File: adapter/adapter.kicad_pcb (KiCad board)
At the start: 2 copper layers, 41.8 x 50.8 mm, 31 parts, among them J1 Serial, J2 Ribbon, J3 RGB, J4 Ribbon, J5 Battery charge, SW1 SW_SPST, SW3 SW_SPDT, U1 Dual MCU: RP2040 + nice!nano, U2 AP1603WG-7

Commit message: pcb: update pcb from schematic
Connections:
- R1 pad 1: +5V -> +3V3
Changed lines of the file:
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@@
 		(tags "net tie solder jumper bridged")
 		(property "Reference" "JP2"
-			(at 0 1.8 360)
+			(at 0 1.8 0)
 			(layer "B.SilkS")
 			(effects
@@
 		)
 		(property "Value" "Jumper_3_Bridged12"
-			(at 0 -1.9 360)
+			(at 0 -1.9 0)
 			(layer "B.Fab")
 			(effects
@@
 		)
 		(fp_text user "3"
-			(at 2.6 0 360)
+			(at 2.6 0 0)
 			(layer "B.SilkS")
 			(effects
@@
 		)
 		(fp_text user "1"
-			(at -2.6 0 360)
+			(at -2.6 0 0)
 			(layer "B.SilkS")
 			(effects
@@
 		(tags "net tie solder jumper bridged")
 		(property "Reference" "JP3"
-			(at 0 1.8 360)
+			(at 0 1.8 0)
 			(layer "B.SilkS")
 			(effects
@@
 		)
 		(property "Value" "Jumper_3_Bridged12"
-			(at 0 -1.9 360)
+			(at 0 -1.9 0)
 			(layer "B.Fab")
 			(effects
@@
 		)
 		(fp_text user "3"
-			(at 2.6 0 360)
+			(at 2.6 0 0)
 			(layer "B.SilkS")
 			(effects
@@
 		)
 		(fp_text user "1"
-			(at -2.6 0 360)
+			(at -2.6 0 0)
 			(layer "B.SilkS")
 			(effects
@@
 			(layers "B.Cu" "B.Paste" "B.Mask")
 			(roundrect_rratio 0.192308)
-			(net 13 "+5V")
+			(net 25 "+3V3")
 			(pintype "passive")
 		)
@@
 		(tags "resistor handsolder")
 		(property "Reference" "R2"
-			(at 0 1.82 270)
+			(at 0 1.82 -90)
 			(layer "B.SilkS")
 			(hide yes)
@@
 		)
 		(property "Value" "2.2k"
-			(at 0 -1.82 270)
+			(at 0 -1.82 -90)
 			(layer "B.Fab")
 			(effects
@@
 		)
 		(fp_text user "${REFERENCE}"
-			(at 0 0 270)
+			(at 0 0 -90)
 			(layer "B.Fab")
 			(effects

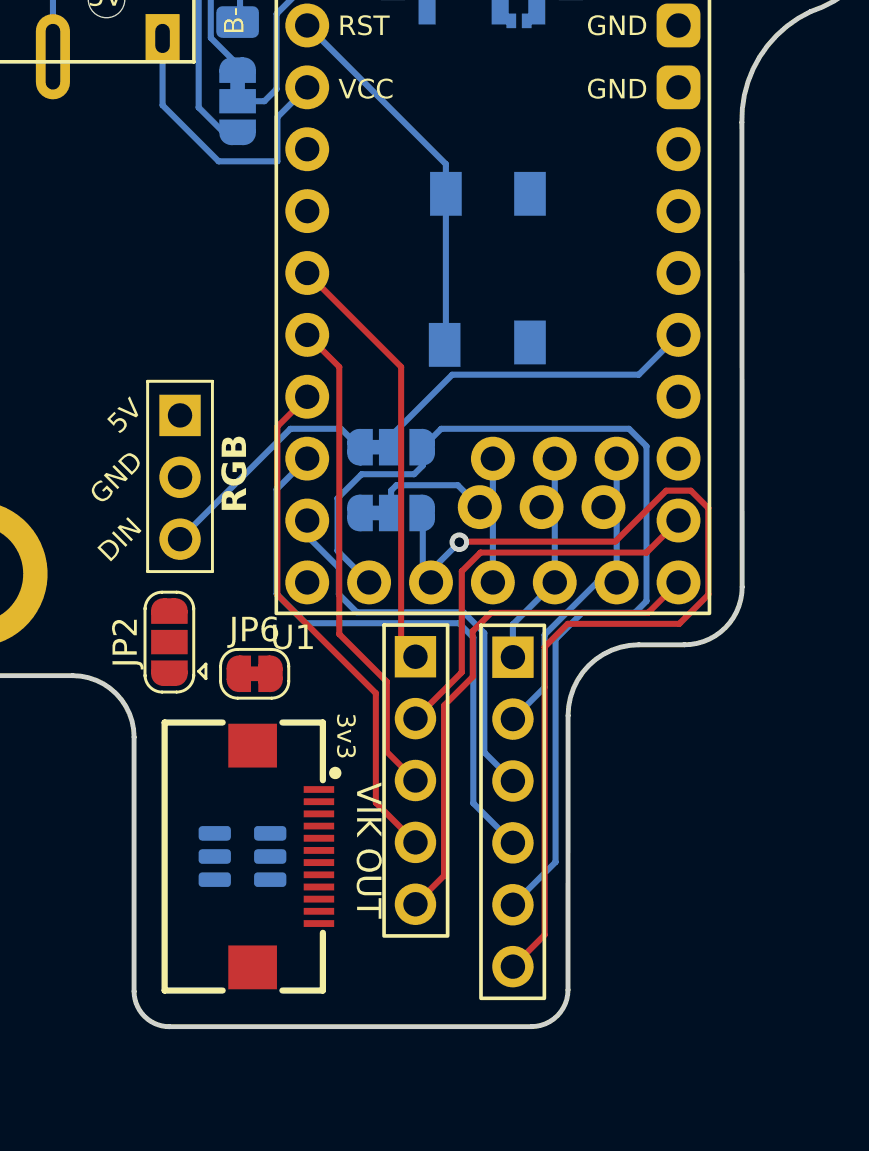
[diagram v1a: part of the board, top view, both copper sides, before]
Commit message: pcb: wire up spi and i2c
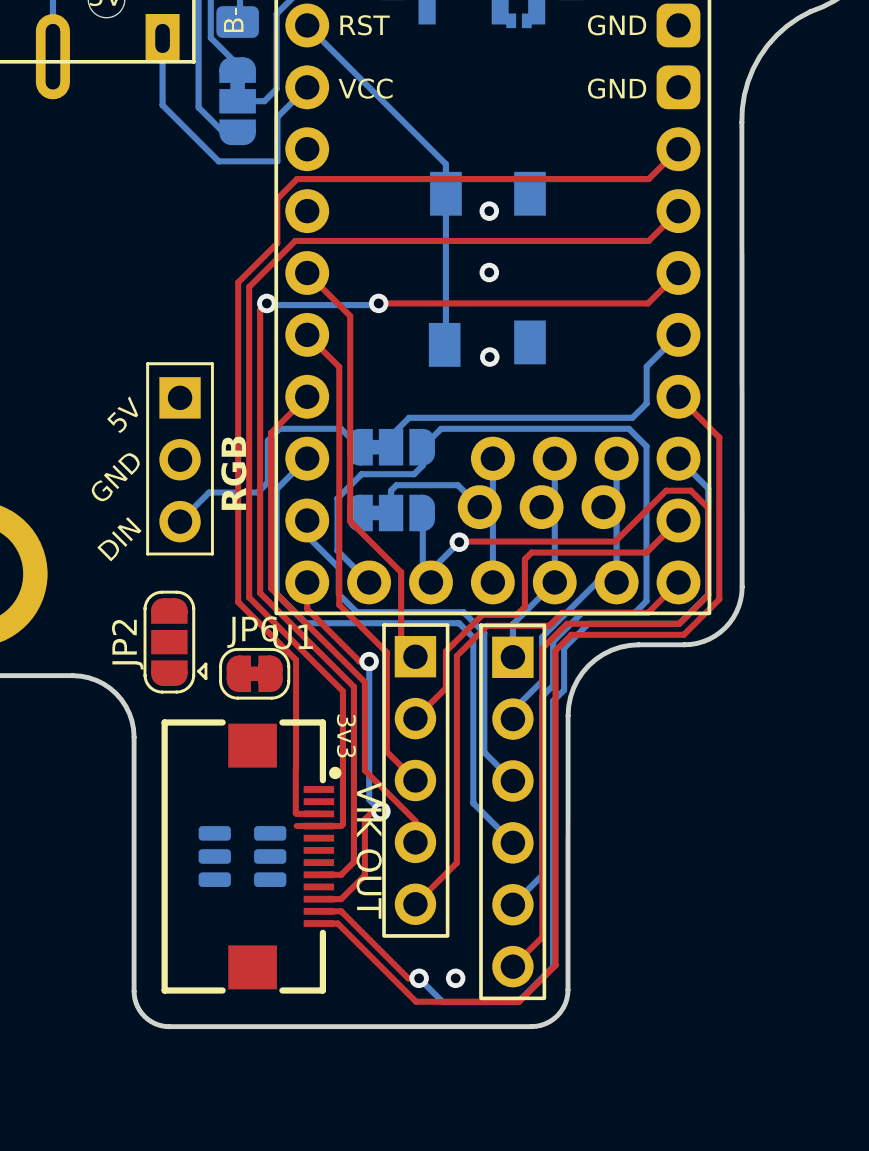
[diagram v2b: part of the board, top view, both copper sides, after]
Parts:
- moved J3 0.72 mm to (125.3, 92.2)
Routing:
- net SDA_L: track 0.00 -> 45.1 mm
- net SCL_L: track 0.00 -> 44.5 mm
- net MOSI_L: track 0.00 -> 43.8 mm, vias 0 -> 2
- net SCLK_L: track 0.00 -> 41.2 mm
- net MISO_L: track 0.00 -> 37.9 mm, vias 0 -> 1
- net SPI_CS_L: track 0.00 -> 16.3 mm, vias 0 -> 2
- net RGB_OR_WL_COL_L: track 14.0 -> 15.2 mm
- net RGB_L: track 9.55 -> 10.3 mm
- net GND: vias 1 -> 5

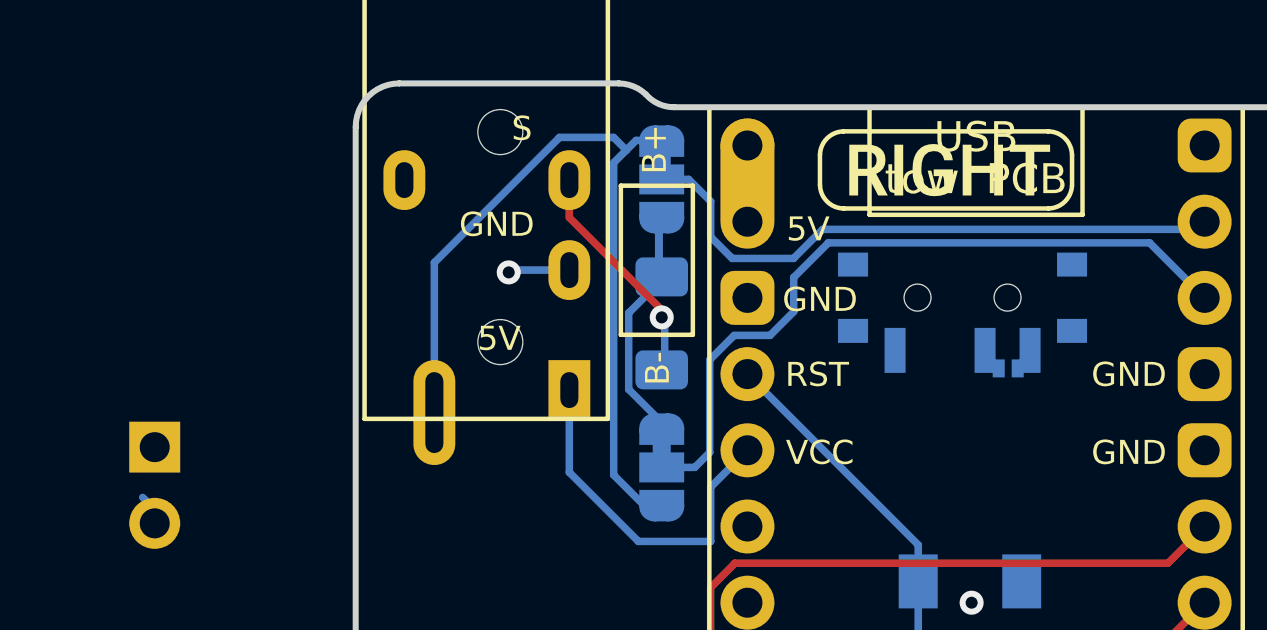
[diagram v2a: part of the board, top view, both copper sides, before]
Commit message: pcb: remove switch. find nicer place for it
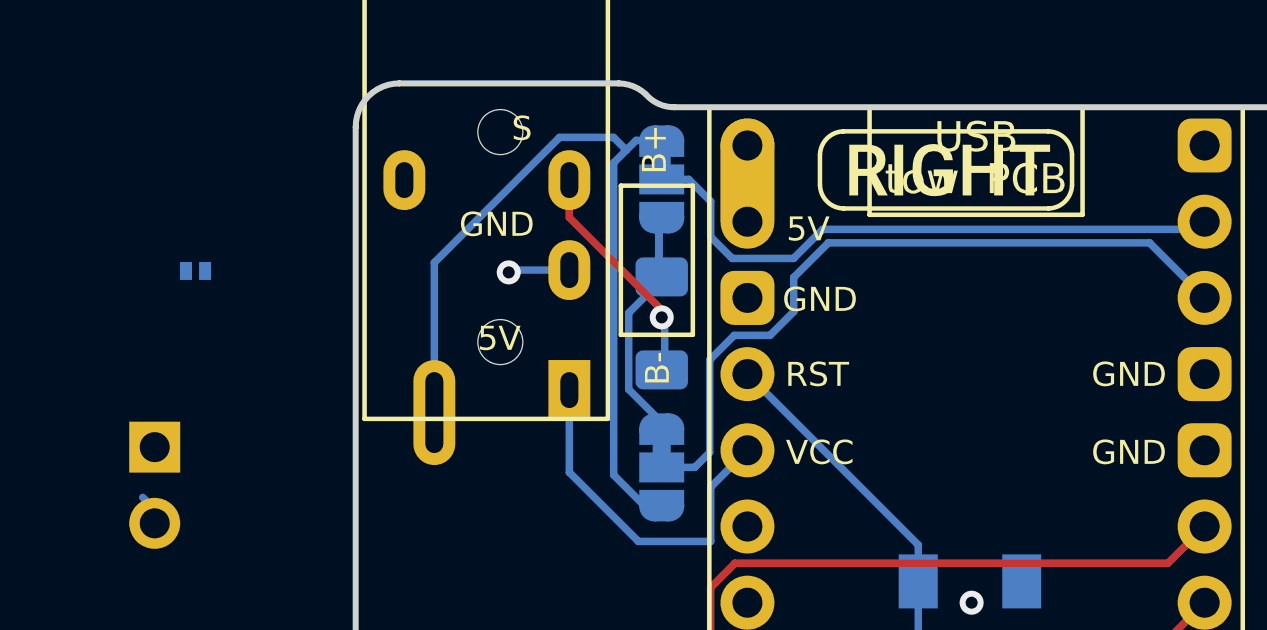
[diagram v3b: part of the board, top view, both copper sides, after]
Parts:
- removed SW3: SW_SPDT, Button_Switch_SMD:SW_SPDT_PCM12
- removed kibuzzard-620B8593: G***, kibuzzard-620B8593
- moved JP1 27.3 mm to (112.2, 73.5)

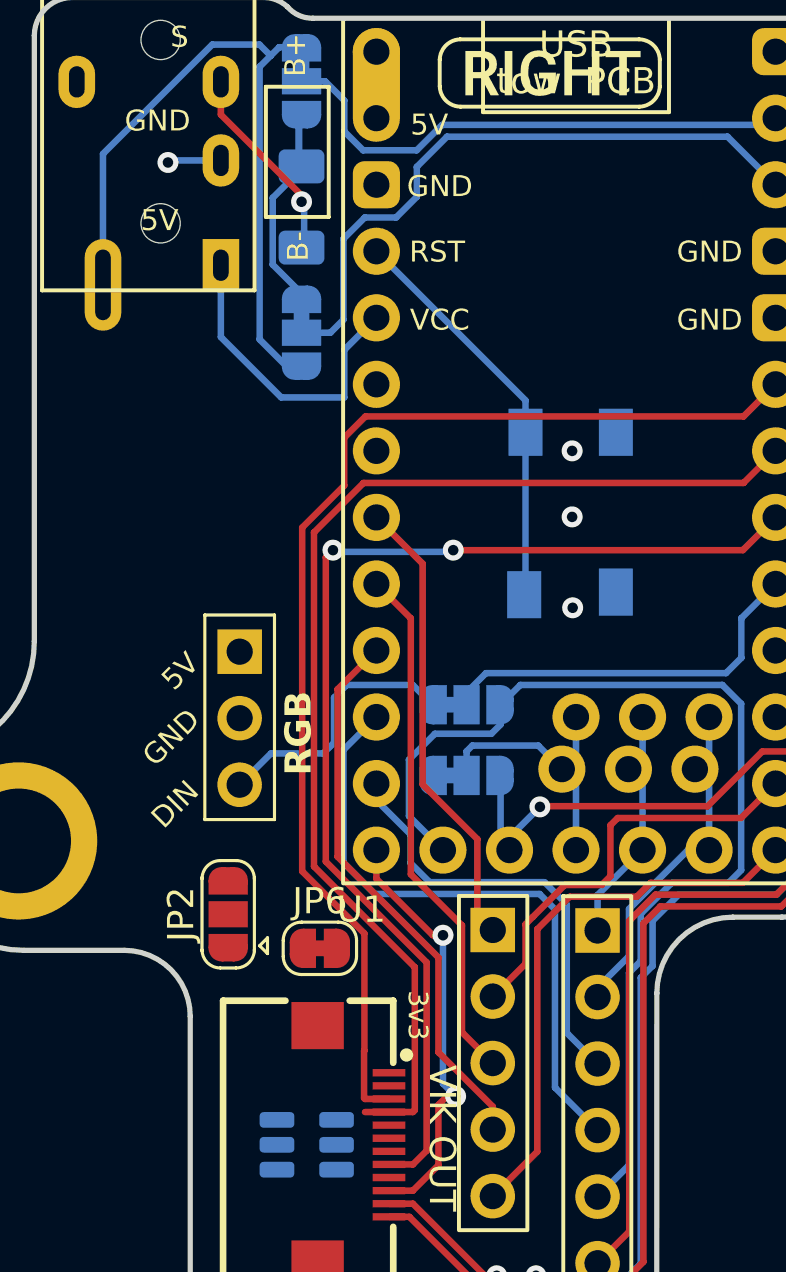
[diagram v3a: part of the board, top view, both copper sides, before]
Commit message: pcb: define thicc netclass group for pwr traces
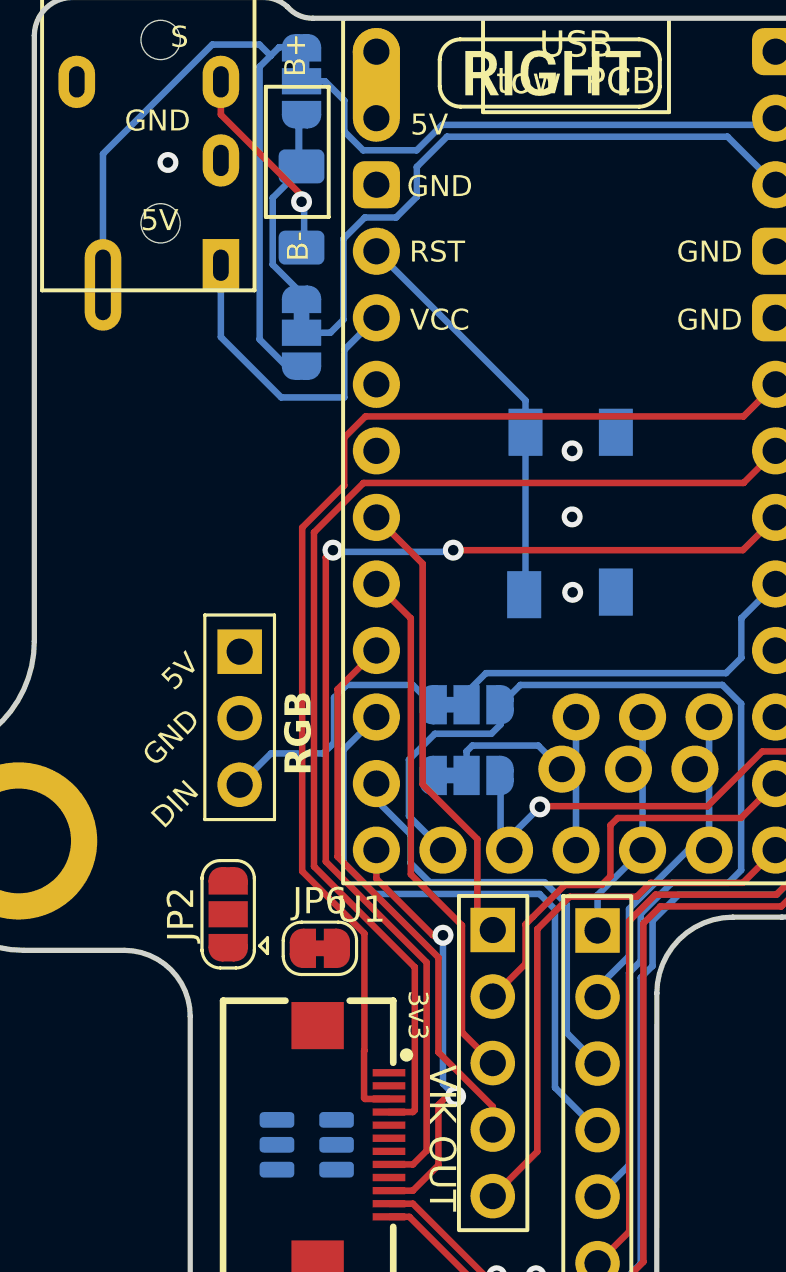
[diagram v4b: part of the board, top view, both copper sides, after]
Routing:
- net GND: track 3.08 -> 1.15 mm
- net SCL_L: track 44.5 -> 43.6 mm
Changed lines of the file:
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@@
 		(at 112.16 73.4525 90)
 		(property "Reference" "JP1"
-			(at 0 1.524 270)
+			(at 0 1.524 -90)
 			(layer "B.SilkS")
 			(hide yes)
@@
 		)
 		(property "Value" "Jumper_2_Open"
-			(at 0 1.389 270)
+			(at 0 1.389 -90)
 			(layer "B.SilkS")
 			(hide yes)
@@
 	)
 	(via
-		(at 138.05 90.5)
+		(at 138.05 89.91)
 		(size 0.8)
 		(drill 0.4)
@@
 	)
 	(segment
-		(start 124.620078 73.42266)
-		(end 122.67734 73.42266)
+		(start 139.69 89.91)
+		(end 139.7 89.9)
 		(width 0.25)
 		(layer "B.Cu")
@@
 		(width 0.25)
 		(layer "F.Cu")
-		(net 18)
-	)
-	(segment
-		(start 131.038 109.75)
-		(end 130.123 109.75)
-		(width 0.25)
-		(layer "F.Cu")

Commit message: pcb: fix up drc
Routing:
- net serial_l: track 10.0 -> 6.42 mm
- net TX_L: track 27.8 -> 29.1 mm
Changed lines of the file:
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@@
 	)
 	(segment
-		(start 126.6 74.85)
-		(end 126.6 77.4)
+		(start 126.36 75.04)
+		(end 126.36 77.36)
 		(width 0.25)
 		(layer "B.Cu")
@@
 	)
 	(segment
-		(start 127.6 73.45)
-		(end 127.8 73.65)
+		(start 127.918198 73.481802)
+		(end 126.36 75.04)
 		(width 0.25)
 		(layer "B.Cu")
@@
 	)
 	(segment
-		(start 127.6 71.7)
-		(end 127.6 73.45)
-		(width 0.25)
-		(layer "B.Cu")
-		(net 14)
-	)
-	(segment
-		(start 127.6 71.7)
-		(end 127.6 73.163604)
-		(width 0.25)
-		(layer "B.Cu")
-		(net 14)
-	)
-	(segment
-		(start 126.6 77.4)
-		(end 127.9 78.7)
-		(width 0.25)
-		(layer "B.Cu")
-		(net 14)
-	)
-	(segment
-		(start 127.6 73.163604)
-		(end 127.918198 73.481802)
-		(width 0.25)
-		(layer "B.Cu")
-		(net 14)
-	)
-	(segment
-		(start 127.8 73.65)
-		(end 126.6 74.85)
+		(start 126.36 77.36)
+		(end 127.7 78.7)
 		(width 0.25)
 		(layer "B.Cu")
@@
 	)
 	(segment
-		(start 126.1 69.845)
-		(end 126.1 80.255)
-		(width 0.25)
-		(layer "B.Cu")
-		(net 33)
-	)
-	(segment
-		(start 126.095 69)
-		(end 126.52 69.425)
+		(start 126.845 69.1)
+		(end 127.7 69.1)
 		(width 0.25)
 		(layer "B.Cu")
@@
 	)
 	(segment
-		(start 126.1 80.255)
-		(end 127.145 81.3)
-		(width 0.25)
-		(layer "B.Cu")
-		(net 33)
-	)
-	(segment
-		(start 127.6 69.1)
-		(end 126.845 69.1)
+		(start 124.293169 69)
+		(end 127.6 69)
 		(width 0.25)
 		(layer "B.Cu")
@@
 	)
 	(segment
-		(start 126.845 69.1)
-		(end 126.52 69.425)
+		(start 125.91 80.065)
+		(end 127.145 81.3)
 		(width 0.25)
 		(layer "B.Cu")
@@
 	)
 	(segment
-		(start 124.293169 69)
-		(end 126.095 69)
+		(start 125.91 70.035)
+		(end 125.91 80.065)
 		(width 0.25)
 		(layer "B.Cu")
@@
 	)
 	(segment
-		(start 126.52 69.425)
-		(end 126.1 69.845)
-		(width 0.25)
-		(layer "B.Cu")
+		(start 127.6 69)
+		(end 127.7 69.1)
+		(width 0.25)
+		(layer "B.Cu")
+		(net 33)
+	)
+	(segment
+		(start 125.91 70.035)
+		(end 126.845 69.1)
+		(width 0.25)
+		(layer "B.Cu")

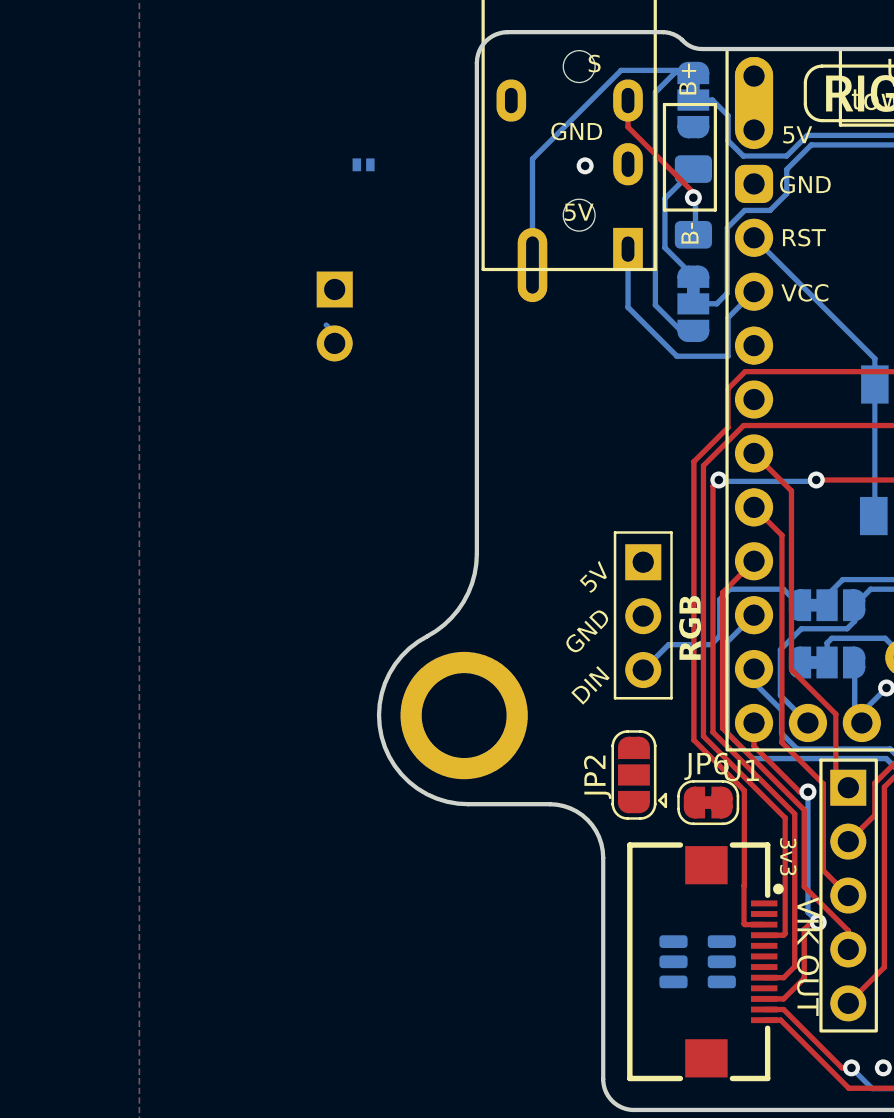
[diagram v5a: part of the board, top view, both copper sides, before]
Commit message: pcb: route vik gpios
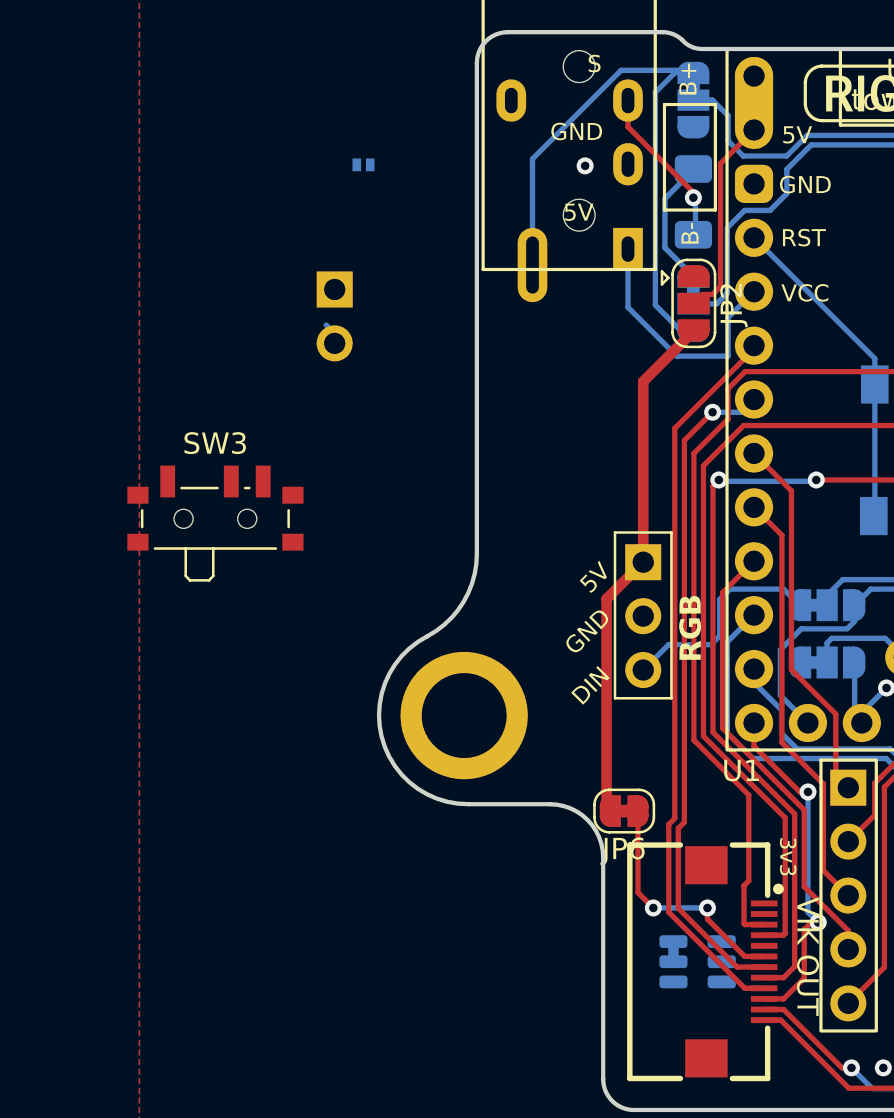
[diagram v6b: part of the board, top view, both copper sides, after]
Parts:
- added SW3: SW_SPDT, Button_Switch_SMD:SW_SPDT_PCM12, F.Cu at (105.2, 89.8)
- moved JP2 22.4 mm to (127.7, 80.0), turned to -90 degrees
- moved JP6 3.98 mm to (124.4, 103.9), turned to 180 degrees
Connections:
- U1 pad 17: GPIO_1_L -> GPIO_2_L
- U1 pad 18: GPIO_2_L -> GPIO_1_L
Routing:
- net GPIO_2_L: track 0.00 -> 34.3 mm
- net GPIO_1_L: track 0.00 -> 31.4 mm, vias 0 -> 1
- net +5V: track 0.00 -> 25.3 mm
- net Net-(J11-5V): track 0.00 -> 11.3 mm, vias 0 -> 2
- net BAT_OR_5V_L: track 0.00 -> 9.62 mm
